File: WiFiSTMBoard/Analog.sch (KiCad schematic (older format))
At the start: 4 parts

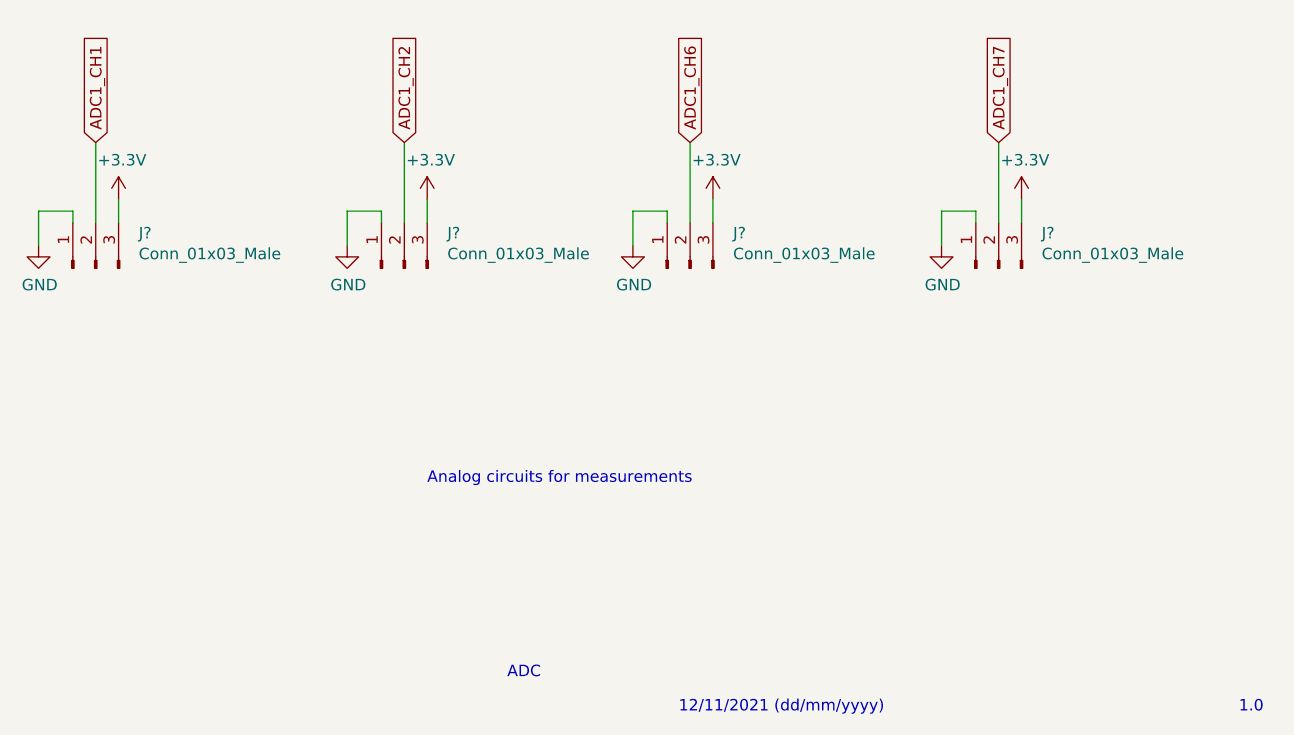
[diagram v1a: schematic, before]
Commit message: finished serial circuit
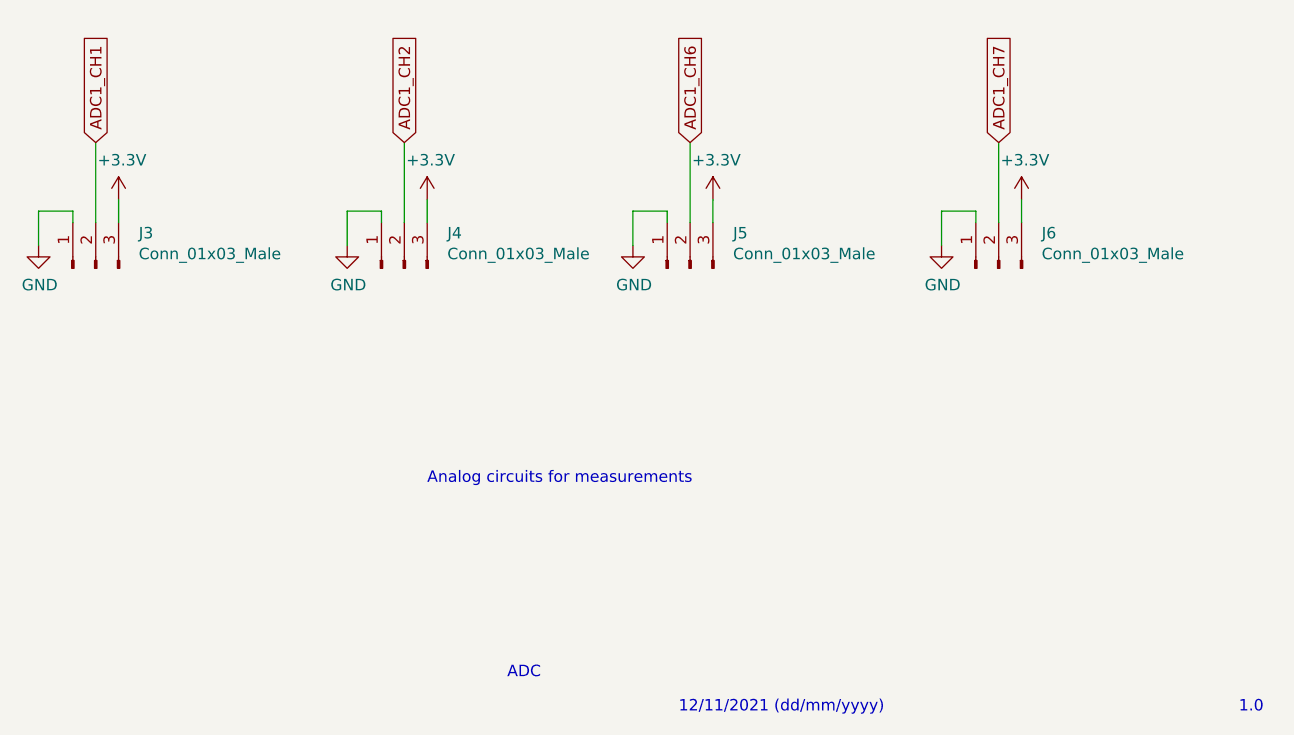
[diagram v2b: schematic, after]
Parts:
- gave numbers to parts that had none: 4
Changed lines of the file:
@@
 1.0
 $Comp
-L Connector:Conn_01x03_Male J?
+L Connector:Conn_01x03_Male J3
 U 1 1 619CAAFB
 P 1750 2150
-F 0 "J?" V 1904 1962 50  0000 R CNN
+F 0 "J3" V 1904 1962 50  0000 R CNN
 F 1 "Conn_01x03_Male" V 1813 1962 50  0000 R CNN
 F 2 "" H 1750 2150 50  0001 C CNN
@@
 $EndComp
 $Comp
-L Connector:Conn_01x03_Male J?
+L Connector:Conn_01x03_Male J4
 U 1 1 619CBBCC
 P 3100 2150
-F 0 "J?" V 3254 1962 50  0000 R CNN
+F 0 "J4" V 3254 1962 50  0000 R CNN
 F 1 "Conn_01x03_Male" V 3163 1962 50  0000 R CNN
 F 2 "" H 3100 2150 50  0001 C CNN
@@
 $EndComp
 $Comp
-L Connector:Conn_01x03_Male J?
+L Connector:Conn_01x03_Male J5
 U 1 1 619CBEC6
 P 4350 2150
-F 0 "J?" V 4504 1962 50  0000 R CNN
+F 0 "J5" V 4504 1962 50  0000 R CNN
 F 1 "Conn_01x03_Male" V 4413 1962 50  0000 R CNN
 F 2 "" H 4350 2150 50  0001 C CNN
@@
 $EndComp
 $Comp
-L Connector:Conn_01x03_Male J?
+L Connector:Conn_01x03_Male J6
 U 1 1 619CC23C
 P 5700 2150
-F 0 "J?" V 5854 1962 50  0000 R CNN
+F 0 "J6" V 5854 1962 50  0000 R CNN
 F 1 "Conn_01x03_Male" V 5763 1962 50  0000 R CNN
 F 2 "" H 5700 2150 50  0001 C CNN
@@
 $EndComp
 $Comp
-L power:GND #PWR?
+L power:GND #PWR0124
 U 1 1 619CD7F8
 P 1500 2050
-F 0 "#PWR?" H 1500 1800 50  0001 C CNN
+F 0 "#PWR0124" H 1500 1800 50  0001 C CNN
 F 1 "GND" H 1505 1877 50  0000 C CNN
 F 2 "" H 1500 2050 50  0001 C CNN
@@
 $EndComp
 $Comp
-L power:GND #PWR?
+L power:GND #PWR0125
 U 1 1 619CDBF6
 P 2850 2050
-F 0 "#PWR?" H 2850 1800 50  0001 C CNN
+F 0 "#PWR0125" H 2850 1800 50  0001 C CNN
 F 1 "GND" H 2855 1877 50  0000 C CNN
 F 2 "" H 2850 2050 50  0001 C CNN
@@
 $EndComp
 $Comp
-L power:GND #PWR?
+L power:GND #PWR0126
 U 1 1 619CE0FE
 P 4100 2050
-F 0 "#PWR?" H 4100 1800 50  0001 C CNN
+F 0 "#PWR0126" H 4100 1800 50  0001 C CNN
 F 1 "GND" H 4105 1877 50  0000 C CNN
 F 2 "" H 4100 2050 50  0001 C CNN
@@
 $EndComp
 $Comp
-L power:GND #PWR?
+L power:GND #PWR0127
 U 1 1 619CEFBA
 P 5450 2050
-F 0 "#PWR?" H 5450 1800 50  0001 C CNN
+F 0 "#PWR0127" H 5450 1800 50  0001 C CNN
 F 1 "GND" H 5455 1877 50  0000 C CNN
 F 2 "" H 5450 2050 50  0001 C CNN
@@
 	5450 1900 5450 2050
 $Comp
-L power:+3.3V #PWR?
+L power:+3.3V #PWR0128
 U 1 1 619D01B0
 P 1850 1850
-F 0 "#PWR?" H 1850 1700 50  0001 C CNN
+F 0 "#PWR0128" H 1850 1700 50  0001 C CNN
 F 1 "+3.3V" H 1865 2023 50  0000 C CNN
 F 2 "" H 1850 1850 50  0001 C CNN
@@
 $EndComp
 $Comp
-L power:+3.3V #PWR?
+L power:+3.3V #PWR0129
 U 1 1 619D0848
 P 3200 1850
-F 0 "#PWR?" H 3200 1700 50  0001 C CNN
+F 0 "#PWR0129" H 3200 1700 50  0001 C CNN
 F 1 "+3.3V" H 3215 2023 50  0000 C CNN
 F 2 "" H 3200 1850 50  0001 C CNN
@@
 $EndComp
 $Comp
-L power:+3.3V #PWR?
+L power:+3.3V #PWR0130
 U 1 1 619D0CCD
 P 4450 1850
-F 0 "#PWR?" H 4450 1700 50  0001 C CNN
+F 0 "#PWR0130" H 4450 1700 50  0001 C CNN
 F 1 "+3.3V" H 4465 2023 50  0000 C CNN
 F 2 "" H 4450 1850 50  0001 C CNN
@@
 $EndComp
 $Comp
-L power:+3.3V #PWR?
+L power:+3.3V #PWR0131
 U 1 1 619D1310
 P 5800 1850
-F 0 "#PWR?" H 5800 1700 50  0001 C CNN
+F 0 "#PWR0131" H 5800 1700 50  0001 C CNN
 F 1 "+3.3V" H 5815 2023 50  0000 C CNN
 F 2 "" H 5800 1850 50  0001 C CNN

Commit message: starting PCB layout
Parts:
- J3, J4, J5, J6: footprint (none) -> Connector_Molex:Molex_KK-396_A-41791-0003_1x03_P3.96mm_Vertical
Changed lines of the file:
@@
 $Descr User 7874 4724
 encoding utf-8
-Sheet 3 6
+Sheet 3 5
 Title ""
 Date ""
@@
 F 0 "J3" V 1904 1962 50  0000 R CNN
 F 1 "Conn_01x03_Male" V 1813 1962 50  0000 R CNN
-F 2 "" H 1750 2150 50  0001 C CNN
+F 2 "Connector_Molex:Molex_KK-396_A-41791-0003_1x03_P3.96mm_Vertical" H 1750 2150 50  0001 C CNN
 F 3 "~" H 1750 2150 50  0001 C CNN
 	1    1750 2150
@@
 F 0 "J4" V 3254 1962 50  0000 R CNN
 F 1 "Conn_01x03_Male" V 3163 1962 50  0000 R CNN
-F 2 "" H 3100 2150 50  0001 C CNN
+F 2 "Connector_Molex:Molex_KK-396_A-41791-0003_1x03_P3.96mm_Vertical" H 3100 2150 50  0001 C CNN
 F 3 "~" H 3100 2150 50  0001 C CNN
 	1    3100 2150
@@
 F 0 "J5" V 4504 1962 50  0000 R CNN
 F 1 "Conn_01x03_Male" V 4413 1962 50  0000 R CNN
-F 2 "" H 4350 2150 50  0001 C CNN
+F 2 "Connector_Molex:Molex_KK-396_A-41791-0003_1x03_P3.96mm_Vertical" H 4350 2150 50  0001 C CNN
 F 3 "~" H 4350 2150 50  0001 C CNN
 	1    4350 2150
@@
 F 0 "J6" V 5854 1962 50  0000 R CNN
 F 1 "Conn_01x03_Male" V 5763 1962 50  0000 R CNN
-F 2 "" H 5700 2150 50  0001 C CNN
+F 2 "Connector_Molex:Molex_KK-396_A-41791-0003_1x03_P3.96mm_Vertical" H 5700 2150 50  0001 C CNN
 F 3 "~" H 5700 2150 50  0001 C CNN
 	1    5700 2150
@@
 $EndComp
 $Comp
-L power:GND #PWR0124
+L power:GND #PWR028
 U 1 1 619CD7F8
 P 1500 2050
-F 0 "#PWR0124" H 1500 1800 50  0001 C CNN
+F 0 "#PWR028" H 1500 1800 50  0001 C CNN
 F 1 "GND" H 1505 1877 50  0000 C CNN
 F 2 "" H 1500 2050 50  0001 C CNN
@@
 $EndComp
 $Comp
-L power:GND #PWR0125
+L power:GND #PWR029
 U 1 1 619CDBF6
 P 2850 2050
-F 0 "#PWR0125" H 2850 1800 50  0001 C CNN
+F 0 "#PWR029" H 2850 1800 50  0001 C CNN
 F 1 "GND" H 2855 1877 50  0000 C CNN
 F 2 "" H 2850 2050 50  0001 C CNN
@@
 $EndComp
 $Comp
-L power:GND #PWR0126
+L power:GND #PWR030
 U 1 1 619CE0FE
 P 4100 2050
-F 0 "#PWR0126" H 4100 1800 50  0001 C CNN
+F 0 "#PWR030" H 4100 1800 50  0001 C CNN
 F 1 "GND" H 4105 1877 50  0000 C CNN
 F 2 "" H 4100 2050 50  0001 C CNN
@@
 $EndComp
 $Comp
-L power:GND #PWR0127
+L power:GND #PWR031
 U 1 1 619CEFBA
 P 5450 2050
-F 0 "#PWR0127" H 5450 1800 50  0001 C CNN
+F 0 "#PWR031" H 5450 1800 50  0001 C CNN
 F 1 "GND" H 5455 1877 50  0000 C CNN
 F 2 "" H 5450 2050 50  0001 C CNN
@@
 	5450 1900 5450 2050
 $Comp
-L power:+3.3V #PWR0128
+L power:+3.3V #PWR024
 U 1 1 619D01B0
 P 1850 1850
-F 0 "#PWR0128" H 1850 1700 50  0001 C CNN
+F 0 "#PWR024" H 1850 1700 50  0001 C CNN
 F 1 "+3.3V" H 1865 2023 50  0000 C CNN
 F 2 "" H 1850 1850 50  0001 C CNN
@@
 $EndComp
 $Comp
-L power:+3.3V #PWR0129
+L power:+3.3V #PWR025
 U 1 1 619D0848
 P 3200 1850
-F 0 "#PWR0129" H 3200 1700 50  0001 C CNN
+F 0 "#PWR025" H 3200 1700 50  0001 C CNN
 F 1 "+3.3V" H 3215 2023 50  0000 C CNN
 F 2 "" H 3200 1850 50  0001 C CNN
@@
 $EndComp
 $Comp
-L power:+3.3V #PWR0130
+L power:+3.3V #PWR026
 U 1 1 619D0CCD
 P 4450 1850
-F 0 "#PWR0130" H 4450 1700 50  0001 C CNN
+F 0 "#PWR026" H 4450 1700 50  0001 C CNN
 F 1 "+3.3V" H 4465 2023 50  0000 C CNN
 F 2 "" H 4450 1850 50  0001 C CNN
@@
 $EndComp
 $Comp
-L power:+3.3V #PWR0131
+L power:+3.3V #PWR027
 U 1 1 619D1310
 P 5800 1850
-F 0 "#PWR0131" H 5800 1700 50  0001 C CNN
+F 0 "#PWR027" H 5800 1700 50  0001 C CNN
 F 1 "+3.3V" H 5815 2023 50  0000 C CNN
 F 2 "" H 5800 1850 50  0001 C CNN

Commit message: .
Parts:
- removed J6: Conn_01x03_Male, Connector_Molex:Molex_KK-396_A-41791-0003_1x03_P3.96mm_Vertical, symbol Connector:Conn_01x03_Male
- J3, J4, J5: footprint Connector_Molex:Molex_KK-396_A-41791-0003_1x03_P3.96mm_Vertical -> Connector_Molex:Molex_Micro-Latch_53253-0370_1x03_P2.00mm_Vertical
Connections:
- net ADC1_CH6 renamed ADC1_CH3
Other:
- moved on the sheet: J3, J4, J5
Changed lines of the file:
@@
 L Connector:Conn_01x03_Male J3
 U 1 1 619CAAFB
-P 1750 2150
-F 0 "J3" V 1904 1962 50  0000 R CNN
-F 1 "Conn_01x03_Male" V 1813 1962 50  0000 R CNN
-F 2 "Connector_Molex:Molex_KK-396_A-41791-0003_1x03_P3.96mm_Vertical" H 1750 2150 50  0001 C CNN
-F 3 "~" H 1750 2150 50  0001 C CNN
-	1    1750 2150
+P 2375 2225
+F 0 "J3" V 2529 2037 50  0000 R CNN
+F 1 "Conn_01x03_Male" V 2438 2037 50  0000 R CNN
+F 2 "Connector_Molex:Molex_Micro-Latch_53253-0370_1x03_P2.00mm_Vertical" H 2375 2225 50  0001 C CNN
+F 3 "~" H 2375 2225 50  0001 C CNN
+	1    2375 2225
 	0    -1   -1   0
 $EndComp
@@
 L Connector:Conn_01x03_Male J4
 U 1 1 619CBBCC
-P 3100 2150
-F 0 "J4" V 3254 1962 50  0000 R CNN
-F 1 "Conn_01x03_Male" V 3163 1962 50  0000 R CNN
-F 2 "Connector_Molex:Molex_KK-396_A-41791-0003_1x03_P3.96mm_Vertical" H 3100 2150 50  0001 C CNN
-F 3 "~" H 3100 2150 50  0001 C CNN
-	1    3100 2150
+P 3725 2225
+F 0 "J4" V 3879 2037 50  0000 R CNN
+F 1 "Conn_01x03_Male" V 3788 2037 50  0000 R CNN
+F 2 "Connector_Molex:Molex_Micro-Latch_53253-0370_1x03_P2.00mm_Vertical" H 3725 2225 50  0001 C CNN
+F 3 "~" H 3725 2225 50  0001 C CNN
+	1    3725 2225
 	0    -1   -1   0
 $EndComp
@@
 L Connector:Conn_01x03_Male J5
 U 1 1 619CBEC6
-P 4350 2150
-F 0 "J5" V 4504 1962 50  0000 R CNN
-F 1 "Conn_01x03_Male" V 4413 1962 50  0000 R CNN
-F 2 "Connector_Molex:Molex_KK-396_A-41791-0003_1x03_P3.96mm_Vertical" H 4350 2150 50  0001 C CNN
-F 3 "~" H 4350 2150 50  0001 C CNN
-	1    4350 2150
-	0    -1   -1   0
-$EndComp
-$Comp
-L Connector:Conn_01x03_Male J6
-U 1 1 619CC23C
-P 5700 2150
-F 0 "J6" V 5854 1962 50  0000 R CNN
-F 1 "Conn_01x03_Male" V 5763 1962 50  0000 R CNN
-F 2 "Connector_Molex:Molex_KK-396_A-41791-0003_1x03_P3.96mm_Vertical" H 5700 2150 50  0001 C CNN
-F 3 "~" H 5700 2150 50  0001 C CNN
-	1    5700 2150
+P 4975 2225
+F 0 "J5" V 5129 2037 50  0000 R CNN
+F 1 "Conn_01x03_Male" V 5038 2037 50  0000 R CNN
+F 2 "Connector_Molex:Molex_Micro-Latch_53253-0370_1x03_P2.00mm_Vertical" H 4975 2225 50  0001 C CNN
+F 3 "~" H 4975 2225 50  0001 C CNN
+	1    4975 2225
 	0    -1   -1   0
 $EndComp
@@
 L power:GND #PWR028
 U 1 1 619CD7F8
-P 1500 2050
-F 0 "#PWR028" H 1500 1800 50  0001 C CNN
-F 1 "GND" H 1505 1877 50  0000 C CNN
-F 2 "" H 1500 2050 50  0001 C CNN
-F 3 "" H 1500 2050 50  0001 C CNN
-	1    1500 2050
+P 2125 2125
+F 0 "#PWR028" H 2125 1875 50  0001 C CNN
+F 1 "GND" H 2130 1952 50  0000 C CNN
+F 2 "" H 2125 2125 50  0001 C CNN
+F 3 "" H 2125 2125 50  0001 C CNN
+	1    2125 2125
 	1    0    0    -1
 $EndComp
@@
 L power:GND #PWR029
 U 1 1 619CDBF6
-P 2850 2050
-F 0 "#PWR029" H 2850 1800 50  0001 C CNN
-F 1 "GND" H 2855 1877 50  0000 C CNN
-F 2 "" H 2850 2050 50  0001 C CNN
-F 3 "" H 2850 2050 50  0001 C CNN
-	1    2850 2050
+P 3475 2125
+F 0 "#PWR029" H 3475 1875 50  0001 C CNN
+F 1 "GND" H 3480 1952 50  0000 C CNN
+F 2 "" H 3475 2125 50  0001 C CNN
+F 3 "" H 3475 2125 50  0001 C CNN
+	1    3475 2125
 	1    0    0    -1
 $EndComp
@@
 L power:GND #PWR030
 U 1 1 619CE0FE
-P 4100 2050
-F 0 "#PWR030" H 4100 1800 50  0001 C CNN
-F 1 "GND" H 4105 1877 50  0000 C CNN
-F 2 "" H 4100 2050 50  0001 C CNN
-F 3 "" H 4100 2050 50  0001 C CNN
-	1    4100 2050
-	1    0    0    -1
-$EndComp
-$Comp
-L power:GND #PWR031
-U 1 1 619CEFBA
-P 5450 2050
-F 0 "#PWR031" H 5450 1800 50  0001 C CNN
-F 1 "GND" H 5455 1877 50  0000 C CNN
-F 2 "" H 5450 2050 50  0001 C CNN
-F 3 "" H 5450 2050 50  0001 C CNN
-	1    5450 2050
+P 4725 2125
+F 0 "#PWR030" H 4725 1875 50  0001 C CNN
+F 1 "GND" H 4730 1952 50  0000 C CNN
+F 2 "" H 4725 2125 50  0001 C CNN
+F 3 "" H 4725 2125 50  0001 C CNN
+	1    4725 2125
 	1    0    0    -1
 $EndComp
 Wire Wire Line
-	1650 1950 1650 1900
+	2275 2025 2275 1975
 Wire Wire Line
-	1650 1900 1500 1900
+	2275 1975 2125 1975
 Wire Wire Line
-	1500 1900 1500 2050
+	2125 1975 2125 2125
 Wire Wire Line
-	3000 1950 3000 1900
+	3625 2025 3625 1975
 Wire Wire Line
-	3000 1900 2850 1900
+	3625 1975 3475 1975
 Wire Wire Line
-	2850 1900 2850 2050
+	3475 1975 3475 2125
 Wire Wire Line
-	4250 1950 4250 1900
+	4875 2025 4875 1975
 Wire Wire Line
-	4250 1900 4100 1900
+	4875 1975 4725 1975
 Wire Wire Line
-	4100 1900 4100 2050
-Wire Wire Line
-	5600 1950 5600 1900
-Wire Wire Line
-	5600 1900 5450 1900
-Wire Wire Line
-	5450 1900 5450 2050
+	4725 1975 4725 2125
 $Comp
 L power:+3.3V #PWR024
 U 1 1 619D01B0
-P 1850 1850
-F 0 "#PWR024" H 1850 1700 50  0001 C CNN
-F 1 "+3.3V" H 1865 2023 50  0000 C CNN
-F 2 "" H 1850 1850 50  0001 C CNN
-F 3 "" H 1850 1850 50  0001 C CNN
-	1    1850 1850
+P 2475 1925
+F 0 "#PWR024" H 2475 1775 50  0001 C CNN
+F 1 "+3.3V" H 2490 2098 50  0000 C CNN
+F 2 "" H 2475 1925 50  0001 C CNN
+F 3 "" H 2475 1925 50  0001 C CNN
+	1    2475 1925
 	1    0    0    -1
 $EndComp
@@
 L power:+3.3V #PWR025
 U 1 1 619D0848
-P 3200 1850
-F 0 "#PWR025" H 3200 1700 50  0001 C CNN
-F 1 "+3.3V" H 3215 2023 50  0000 C CNN
-F 2 "" H 3200 1850 50  0001 C CNN
-F 3 "" H 3200 1850 50  0001 C CNN
-	1    3200 1850
+P 3825 1925
+F 0 "#PWR025" H 3825 1775 50  0001 C CNN
+F 1 "+3.3V" H 3840 2098 50  0000 C CNN
+F 2 "" H 3825 1925 50  0001 C CNN
+F 3 "" H 3825 1925 50  0001 C CNN
+	1    3825 1925
 	1    0    0    -1
 $EndComp
@@
 L power:+3.3V #PWR026
 U 1 1 619D0CCD
-P 4450 1850
-F 0 "#PWR026" H 4450 1700 50  0001 C CNN
-F 1 "+3.3V" H 4465 2023 50  0000 C CNN
-F 2 "" H 4450 1850 50  0001 C CNN
-F 3 "" H 4450 1850 50  0001 C CNN
-	1    4450 1850
-	1    0    0    -1
-$EndComp
-$Comp
-L power:+3.3V #PWR027
-U 1 1 619D1310
-P 5800 1850
-F 0 "#PWR027" H 5800 1700 50  0001 C CNN
-F 1 "+3.3V" H 5815 2023 50  0000 C CNN
-F 2 "" H 5800 1850 50  0001 C CNN
-F 3 "" H 5800 1850 50  0001 C CNN
-	1    5800 1850
+P 5075 1925
+F 0 "#PWR026" H 5075 1775 50  0001 C CNN
+F 1 "+3.3V" H 5090 2098 50  0000 C CNN
+F 2 "" H 5075 1925 50  0001 C CNN
+F 3 "" H 5075 1925 50  0001 C CNN
+	1    5075 1925
 	1    0    0    -1
 $EndComp
 Wire Wire Line
-	1850 1950 1850 1850
+	2475 2025 2475 1925
 Wire Wire Line
-	3200 1950 3200 1850
+	3825 2025 3825 1925
 Wire Wire Line
-	4450 1950 4450 1850
-Wire Wire Line
-	5800 1950 5800 1850
-Text GLabel 1750 1600 1    50   Input ~ 0
+	5075 2025 5075 1925
+Text GLabel 2375 1675 1    50   Input ~ 0
 ADC1_CH1
 Wire Wire Line
-	1750 1600 1750 1950
-Text GLabel 3100 1600 1    50   Input ~ 0
+	2375 1675 2375 2025
+Text GLabel 3725 1675 1    50   Input ~ 0
 ADC1_CH2
 Wire Wire Line
-	3100 1600 3100 1950
-Text GLabel 4350 1600 1    50   Input ~ 0
-ADC1_CH6
+	3725 1675 3725 2025
+Text GLabel 4975 1675 1    50   Input ~ 0
+ADC1_CH3
 Wire Wire Line
-	4350 1950 4350 1600
-Text GLabel 5700 1600 1    50   Input ~ 0
-ADC1_CH7
-Wire Wire Line
-	5700 1950 5700 1600
+	4975 2025 4975 1675
 $EndSCHEMATC
